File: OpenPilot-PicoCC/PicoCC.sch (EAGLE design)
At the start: 76 parts, among them U1 STM32F103CBT6, U3 LM4120AIM5-1.8, U4 LT6654AHS6-3.3TRMPBF, U5 L3G4200D, X1 MINI-USB-SCHIELD-32005-301, X2 08FLZ-SM1

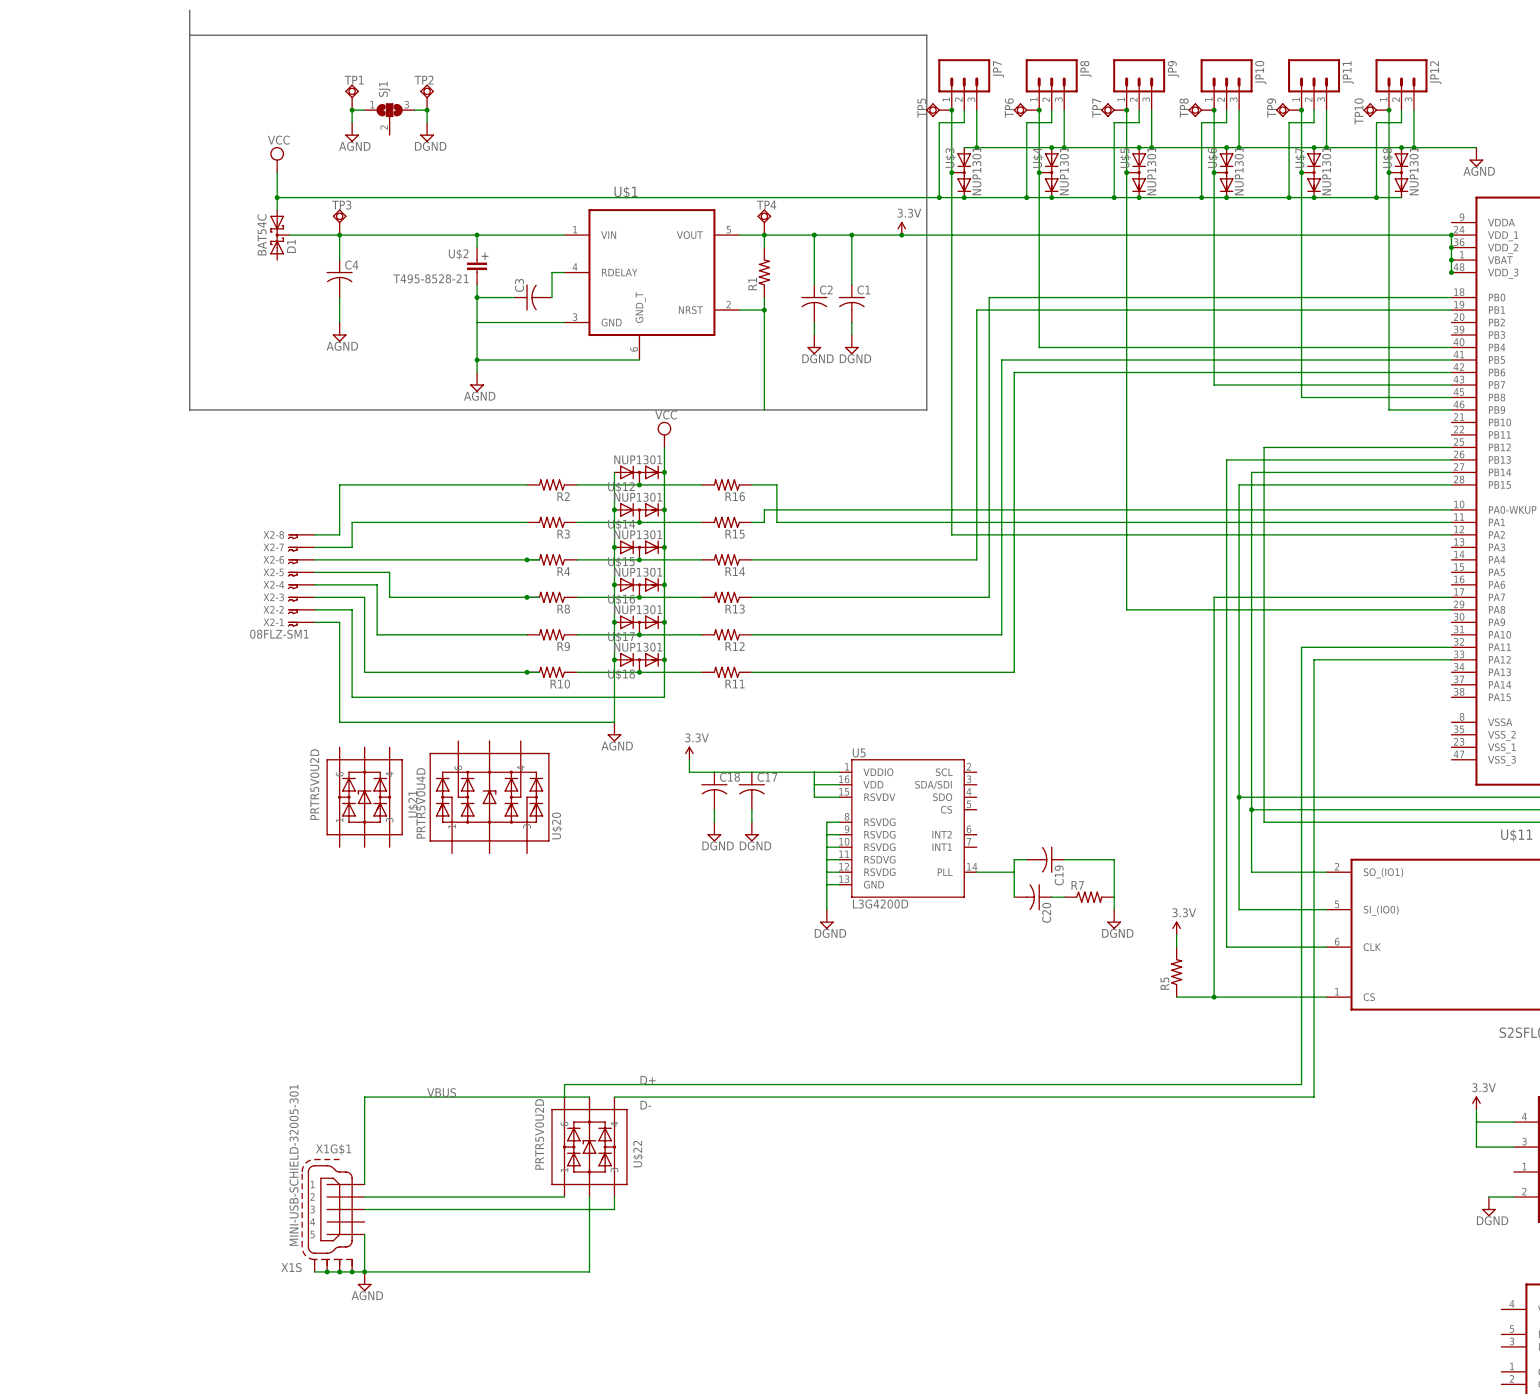
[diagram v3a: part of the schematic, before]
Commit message: Reduced ESD components by combining RC Input and USB
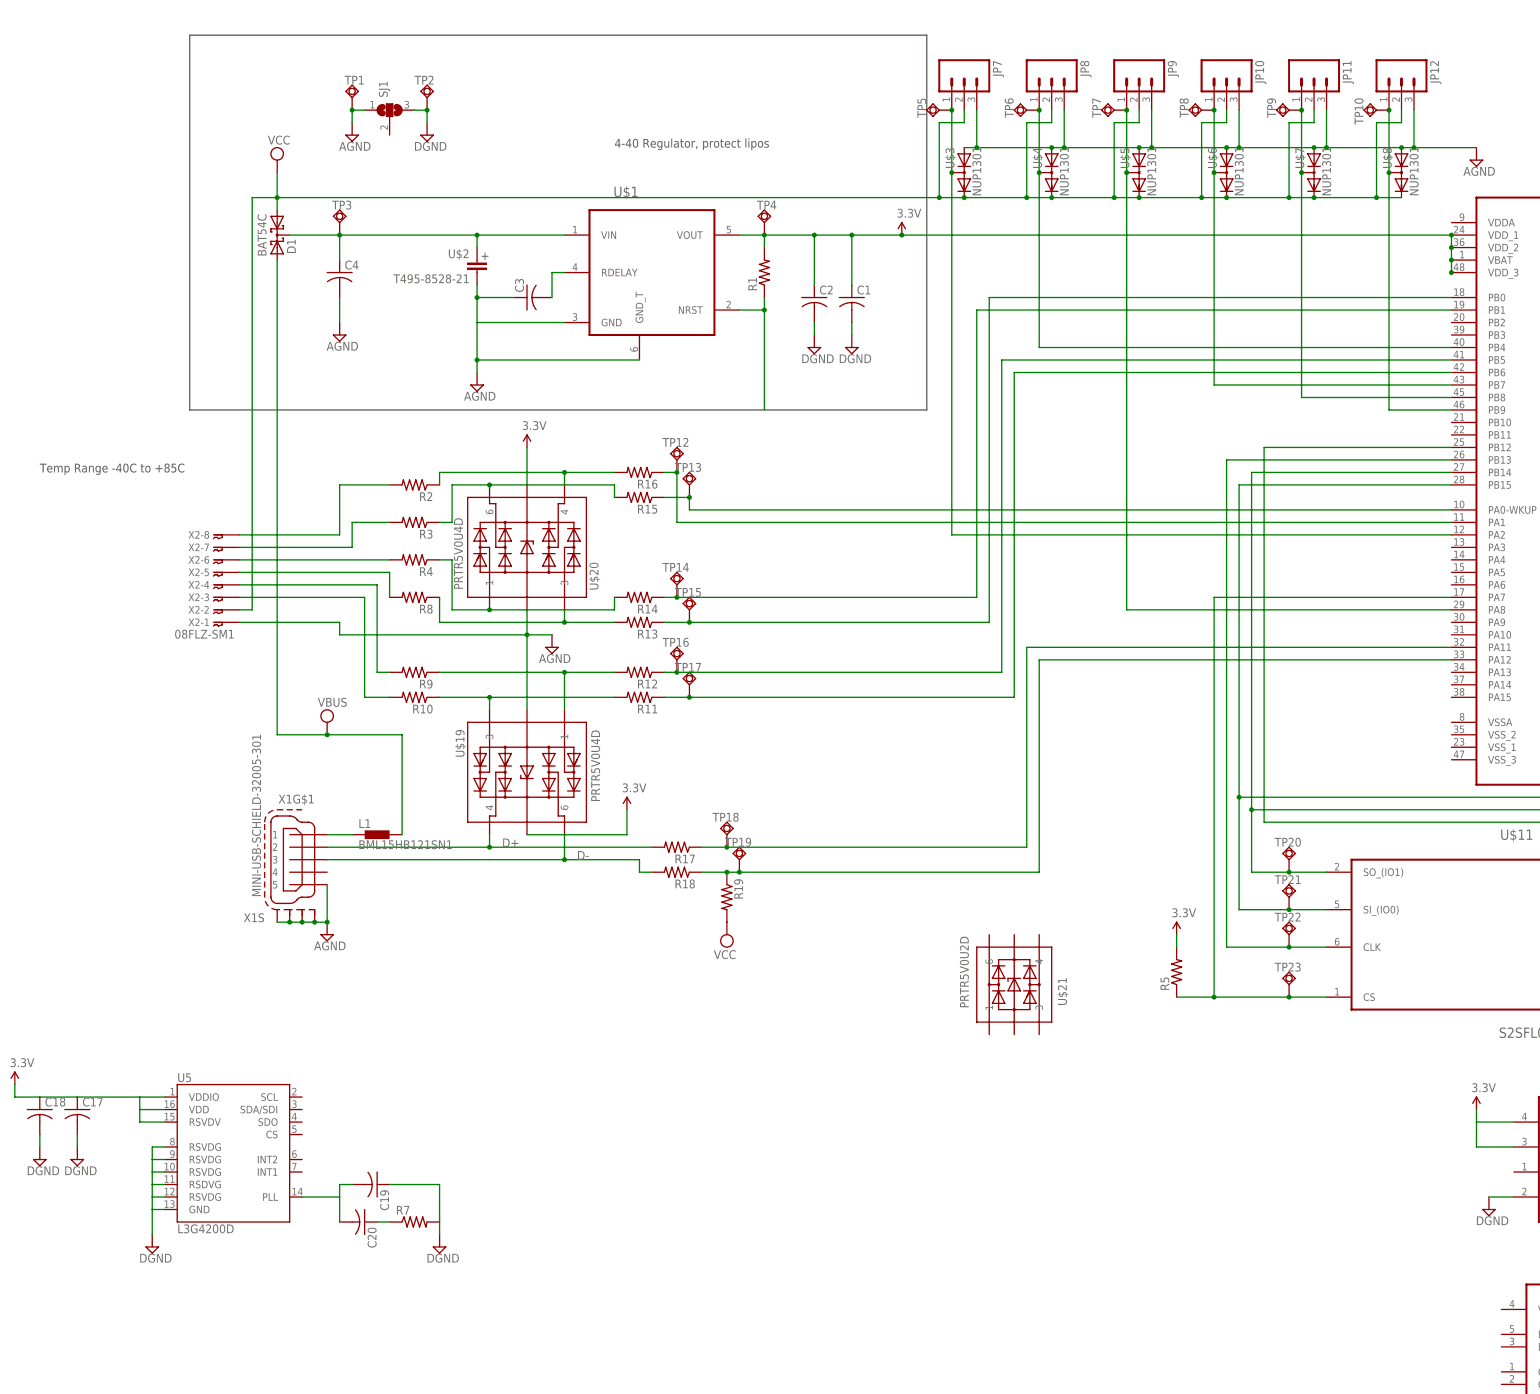
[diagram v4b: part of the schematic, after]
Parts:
- removed U$12, U$14, U$15, U$16, U$17, U$18: NUP1301, NXP:NUP1301
- removed U$22: PRTR5V0U2D, NXP:PRTR5V0U2D
- added L1: BML15HB121SN1, inductors:BML15HB121SN1
- added R17, R18, R19: (no value), rcl:R-US_R0402
- added TP12, TP13, TP14, TP15, TP16, TP17, TP18, TP19, TP20, TP21, TP22, TP23: TPSQTP12R, testpad:TPSQTP12R
- added U$19: PRTR5V0U4D, NXP:PRTR5V0U4D
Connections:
- removed net N$2: U$22.1, X1G$1.2
- removed net N$20: R15.2, R3.1, U$14.3
- removed net N$21: R14.2, R4.1, U$15.3
- removed net N$26: R13.2, R8.1, U$16.3
- removed net N$27: R12.2, R9.1, U$17.3
- removed net N$28: R10.1, R11.2, U$18.3
- removed net N$5: U$22.3, X1G$1.3
- removed net VBUS: U$22.5, X1G$1.1
- new net D+2: R17.1, TP18.TP, U1.PA11
- new net D-2: R18.1, R19.1, TP19.TP, U1.PA12
- new net N$36: R16.2, R2.1, U$20.4
- new net N$39: R14.2, R4.1, U$20.1
- new net N$42: R13.2, R8.1, U$20.3
- new net N$44: R10.1, R11.2, U$19.3
- new net N$45: R12.2, R9.1, U$19.1
- net 3.3V: now also R15.2, R3.1, U$19.5, U$20.6
- net AGND: now also U$19.2, U$20.2; no longer U$12.1, U$14.1, U$15.1, U$16.1, U$17.1, U$18.1, U$22.2
- net D+: now also R17.2, U$19.4, X1G$1.2; no longer U$22.6, U1.PA11
- net D-: now also R18.2, U$19.6, X1G$1.3; no longer U$22.4, U1.PA12
- net N$1: now also L1.1, X1G$1.1; no longer R16.2, R2.1, U$12.3
- net N$15: now also TP23.TP
- net N$16: now also TP22.TP
- net N$17: now also TP21.TP
- net N$18: now also TP20.TP
- net N$30: now also TP12.TP
- net N$31: now also TP13.TP
- net N$32: now also TP14.TP
- net N$33: now also TP15.TP
- net N$34: now also TP16.TP
- net N$35: now also TP17.TP
- net VCC: now also D1.A2, L1.2, R19.2; no longer U$12.2, U$14.2, U$15.2, U$16.2, U$17.2, U$18.2
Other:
- note added: "4-40 Regulator, protect lipos"
- note added: "Temp Range -40C to +85C"
- moved on the sheet: C17, C18, C19, C20, R10, R11, R12, R13, R14, R15, R16, R2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

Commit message: Decided on three levels for structural integrity and modularity. Setup the second source for Analog and raw power. Need secondary LDO for increase sensor stability.
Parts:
- removed C16: (no value), rcl:C-USC0402K
- removed U3: LM4120AIM5-1.8, national-semiconductor:LM4120AIM5-1.8
- removed U4: LT6654AHS6-3.3TRMPBF, linear-technology:LT6654AHS6-3.3TRMPBF
- added C10, C9: (no value), rcl:C-USC0402
- added C11: (no value), rcl:C-USC0402K
- added R20: (no value), rcl:R-US_R0402
- added SJ2, SJ3: (no value), jumper:SJ2WW
- added TP24, TP25, TP26, TP27, TP28, TP29: TPSQTP12R, testpad:TPSQTP12R
- added U$14: T495-8528-21, Kemet:T495-8528-21
- added U$15: (no value), TI_TPS:TPS7A6033-Q1
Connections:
- removed net N$3: C4.1, D1.CC, TP3.TP, U$1.VIN, U$2.1
- new net N$2: C4.1, D1.CC, TP28.TP, TP3.TP, U$1.VIN, U$14.1, U$15.VIN, U$2.1
- new net N$5: C11.2, U$15.RDELAY
- new net N$7: R20.1, U$15.NRST
- net 3.3V: no longer U3.EN, U3.VIN
- net AGND: now also C11.1, SJ2.1, SJ3.1, TP24.TP, TP26.TP, U$14.2, U$15.GND, U$15.GND_T
- net DGND: now also C10.2, C9.2, SJ2.3, SJ3.3, TP25.TP, TP27.TP; no longer C16.2, U3.GND
- net VEE: now also C10.1, C9.1, R20.2, TP29.TP, U$15.VOUT, U1.VDDA; no longer C16.1, U3.VOUT
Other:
- note added: "Power Level"
- note added: "Sensor Level"
- moved on the sheet: C17, C18, C19, C20, R7, SJ1, TP1, TP2, TP3, U5

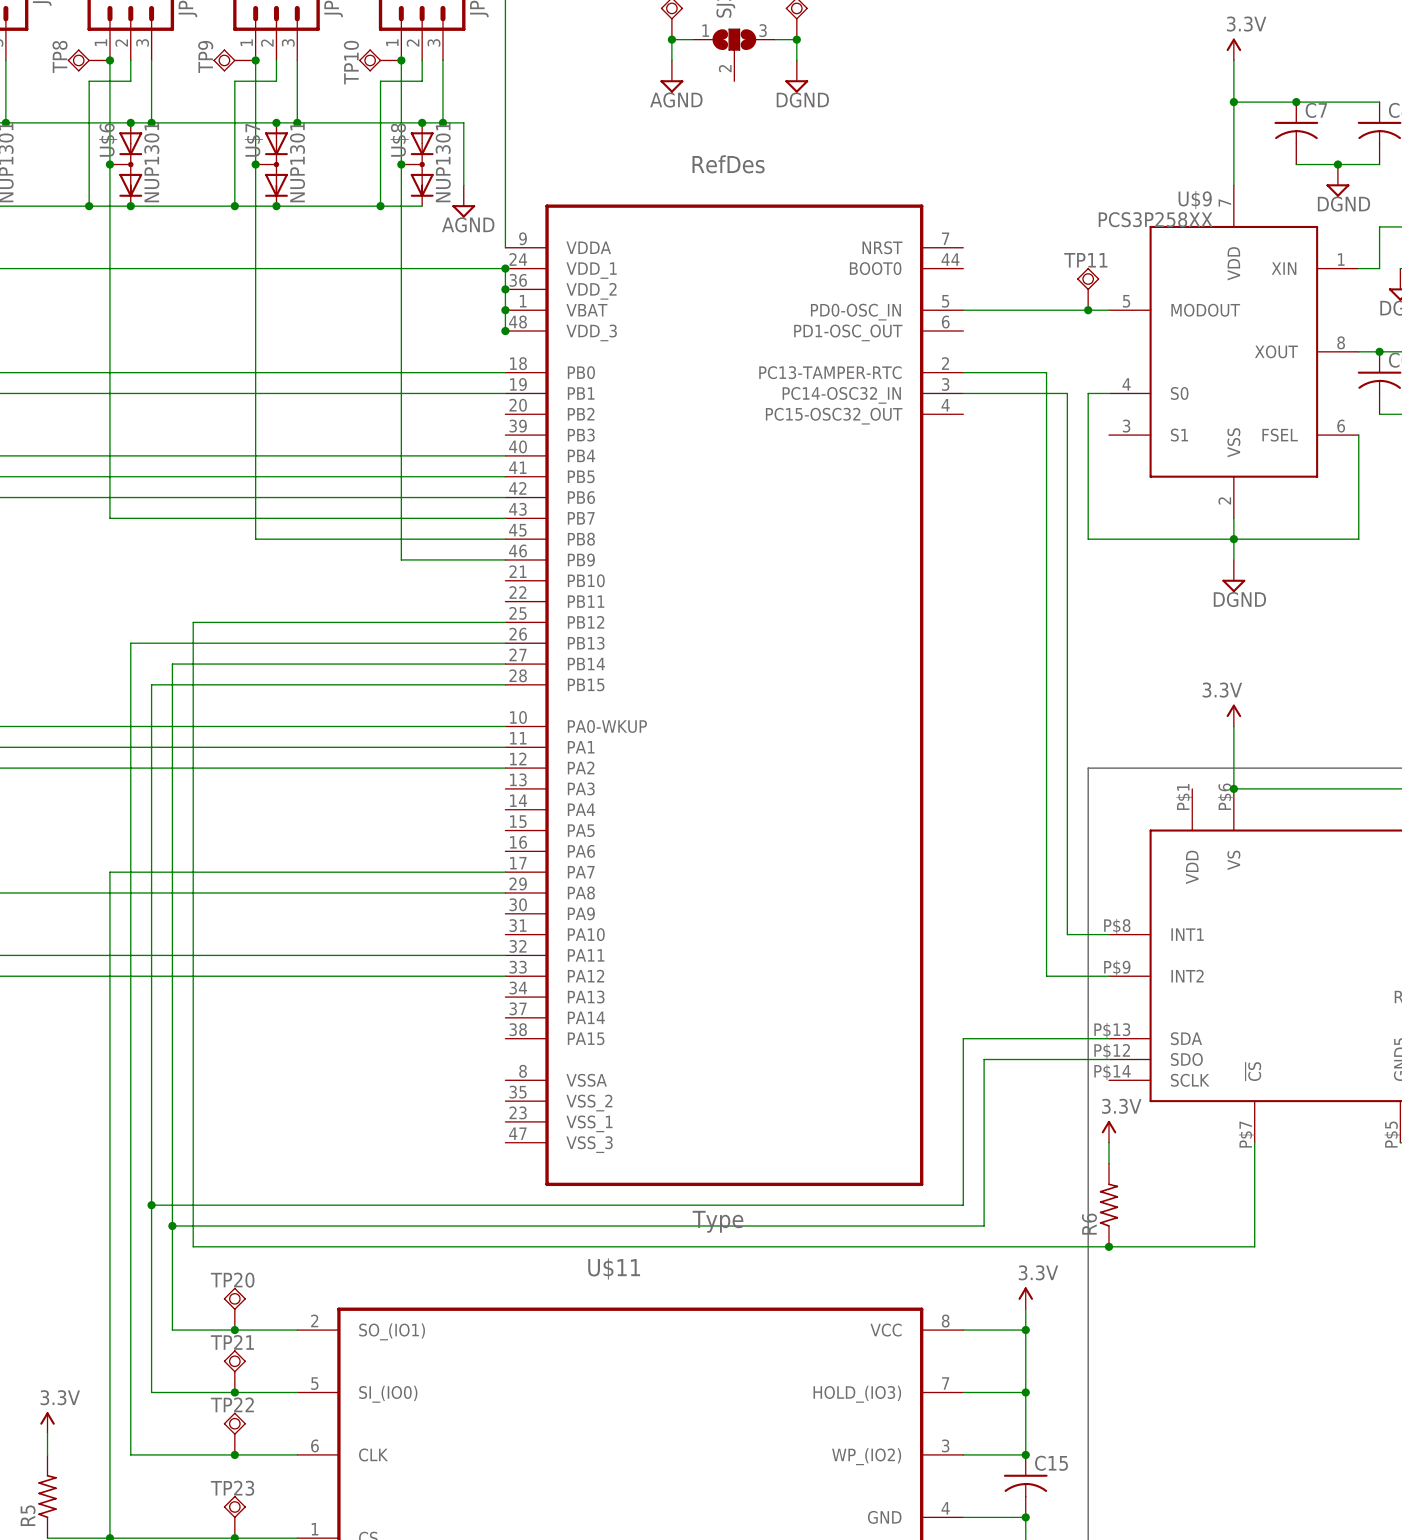
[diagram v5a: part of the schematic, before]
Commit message: Switched to the 64 pin STM23 to implement the F1->F4 compatability path.
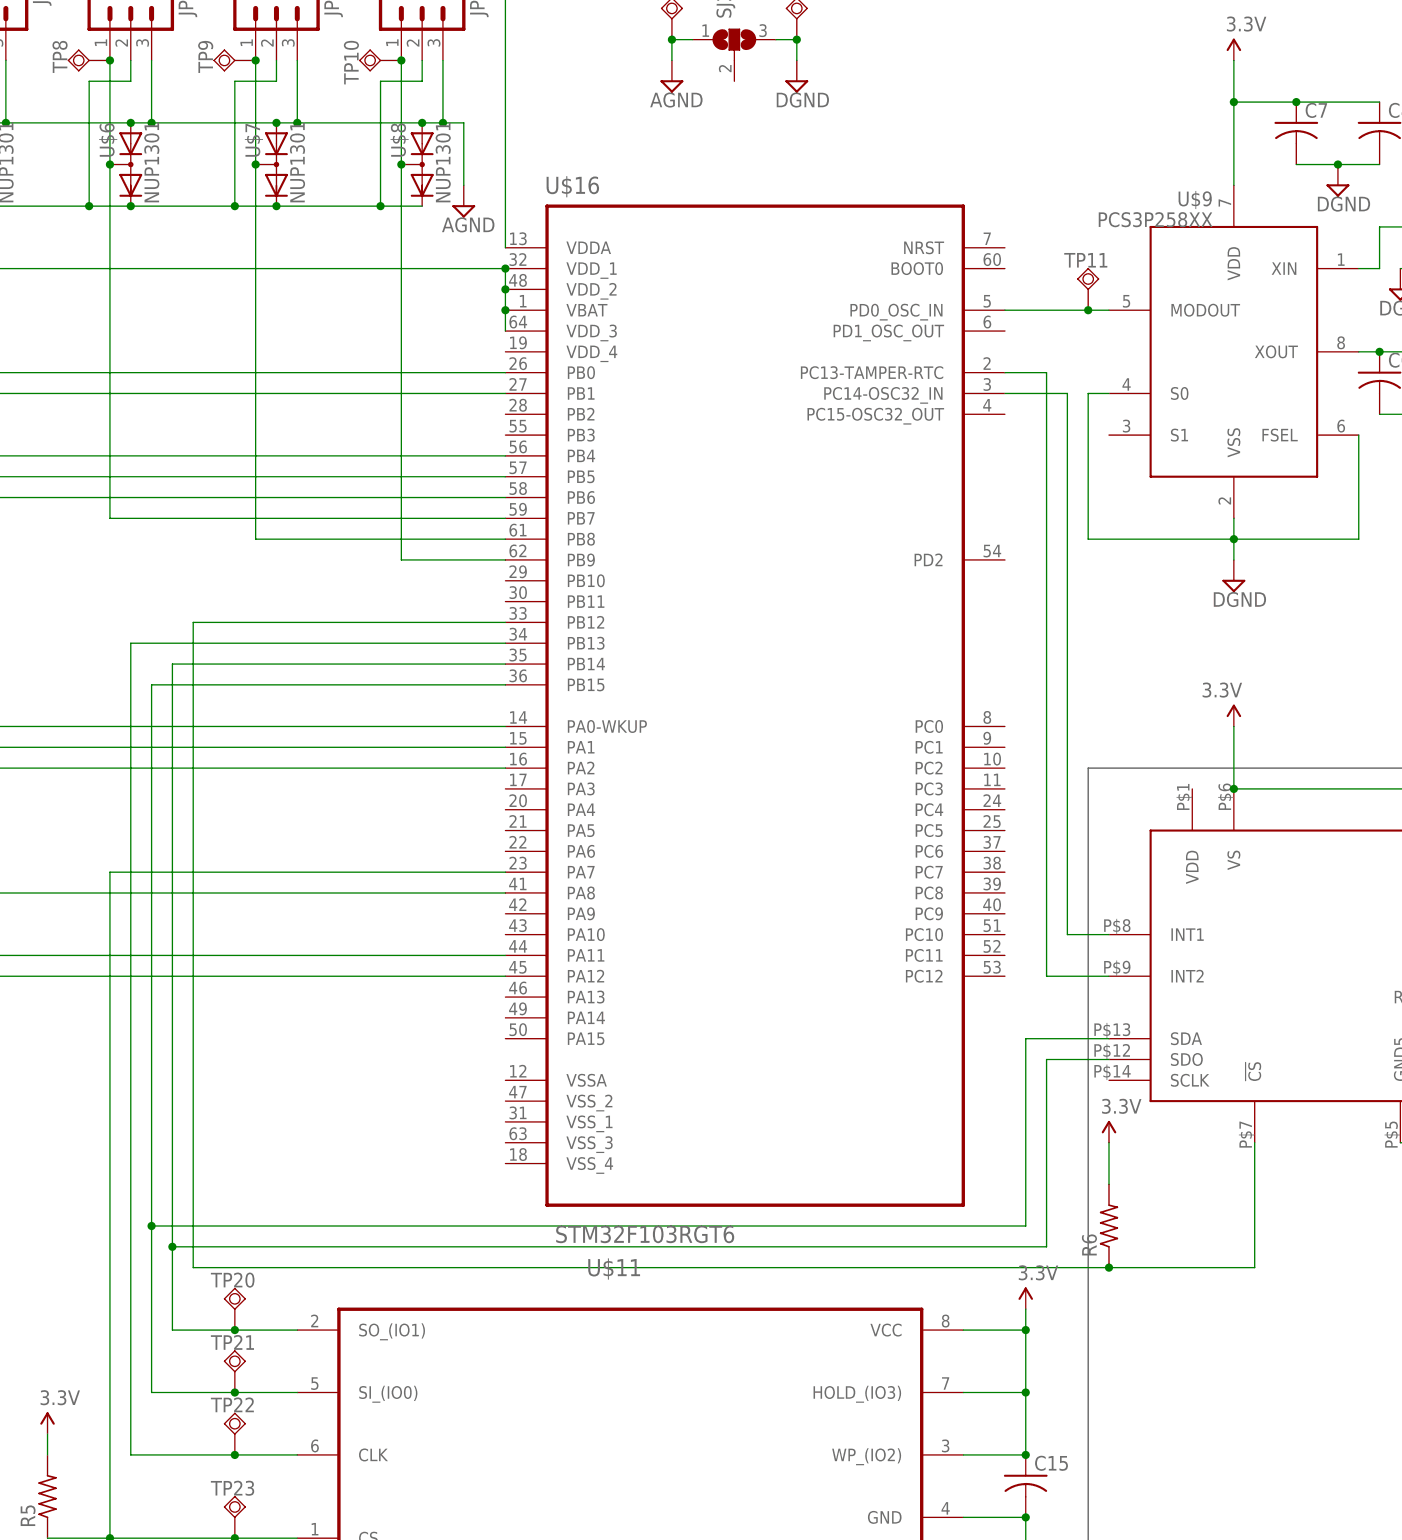
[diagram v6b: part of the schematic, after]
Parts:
- removed U1: STM32F103CBT6, st-microelectronics:STM32F103CBT6
- added U$16: STM32F103RGT6, st-microelectronics:STM32F103RGT6
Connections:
- net 3.3V: now also U$16.VBAT, U$16.VDD_1, U$16.VDD_2, U$16.VDD_3; no longer U1.VBAT, U1.VDD_1, U1.VDD_2, U1.VDD_3
- net D+2: now also U$16.PA11; no longer U1.PA11
- net D-2: now also U$16.PA12; no longer U1.PA12
- net N$10: now also U$16.PA8; no longer U1.PA8
- net N$11: now also U$16.PB7; no longer U1.PB7
- net N$12: now also U$16.PB8; no longer U1.PB8
- net N$13: now also U$16.PB9; no longer U1.PB9
- net N$14: now also U$16.PD0_OSC_IN; no longer U1.PD0-OSC_IN
- net N$15: now also U$16.PA7; no longer U1.PA7
- net N$16: now also U$16.PB13; no longer U1.PB13
- net N$17: now also U$16.PB15; no longer U1.PB15
- net N$18: now also U$16.PB14; no longer U1.PB14
- net N$30: now also U$16.PA1; no longer U1.PA1
- net N$31: now also U$16.PA0-WKUP; no longer U1.PA0-WKUP
- net N$32: now also U$16.PB1; no longer U1.PB1
- net N$33: now also U$16.PB0; no longer U1.PB0
- net N$34: now also U$16.PB5; no longer U1.PB5
- net N$35: now also U$16.PB6; no longer U1.PB6
- net N$40: now also U$16.PC14-OSC32_IN; no longer U1.PC14-OSC32_IN
- net N$41: now also U$16.PC13-TAMPER-RTC; no longer U1.PC13-TAMPER-RTC
- net N$43: now also U$16.PB12; no longer U1.PB12
- net N$8: now also U$16.PA2; no longer U1.PA2
- net N$9: now also U$16.PB4; no longer U1.PB4
- net VEE: now also U$16.VDDA; no longer U1.VDDA
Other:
- moved on the sheet: R6
